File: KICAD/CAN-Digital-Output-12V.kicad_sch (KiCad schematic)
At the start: 26 parts, among them J1 UPDI Header, J2 Conn_01x04_Female, J3 UART Header, U1 AZ1117-5.0, U2 MCP2551-I-SN, U3 ATtiny414-SS, U5 MCP2515-xSO, Y1 8MHz

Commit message: Design review with Jarrod
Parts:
- added J4: 0367831201, 0367831201:MOLEX_0367831201, symbol 0367831201:0367831201
- added R10, R6, R8, R9: 1K, Resistor_SMD:R_0603_1608Metric_Pad0.98x0.95mm_HandSolder, symbol Device:R
- added U4, U6, U7, U8: VNL5050N3TR-E, Package_TO_SOT_SMD:SOT-223, symbol VNL5050N3TR-E:VNL5050N3TR-E
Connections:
- net CAN_H: now also J4.11
- net CAN_L: now also J4.12
- net GND: now also J4.4, J4.5, J4.6, U4.3 (SOURCE), U6.3 (SOURCE), U7.3 (SOURCE), U8.3 (SOURCE)
- net OUT_1: now also R6.1
- net OUT_2: now also R8.1
- net OUT_3: now also R9.1
- net OUT_4: now also R10.1
- net VCC: now also J4.1, J4.2, J4.3
- new net: R6.2, U4.1 (INPUT)
- new net: R8.2, U6.1 (INPUT)
- new net: R9.2, U7.1 (INPUT)
- new net: R10.2, U8.1 (INPUT)
- new net DO_1: J4.7, U4.2 (DRAIN), U4.4 (DRAIN)
- new net DO_2: J4.8, U6.2 (DRAIN), U6.4 (DRAIN)
- new net DO_3: J4.9, U7.2 (DRAIN), U7.4 (DRAIN)
- new net DO_4: J4.10, U8.2 (DRAIN), U8.4 (DRAIN)
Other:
- note added: "* Add LED indicator for Switches"
- note removed: "* Add LED indicator for Relays"
- moved on the sheet: H1, H2, H3, H4

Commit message: Third Design Review
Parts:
- removed J2: Conn_01x04_Female, Connector_PinHeader_1.27mm:PinHeader_1x04_P1.27mm_Vertical, symbol Connector:Conn_01x04_Female
- added D1, D2, D3, D4: LED, LED_SMD:LED_0603_1608Metric_Pad1.05x0.95mm_HandSolder, symbol Device:LED
- added R11, R12, R13, R14: 150, Resistor_SMD:R_0603_1608Metric_Pad0.98x0.95mm_HandSolder, symbol Device:R
- added S1: 219-4MSTR, 219-4MSTR:SOP254P991X385-8N, symbol 219-4MSTR:219-4MSTR
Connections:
- net GND: now also R11.1, R12.1, R13.1, R14.1
- net OUT_1: now also D1.2 (A)
- net OUT_2: now also D2.2 (A)
- net OUT_3: now also D3.2 (A)
- net OUT_4: now also D4.2 (A)
- new net: D1.1 (K), R11.2
- new net: D3.1 (K), R13.2
- new net: D2.1 (K), R12.2
- new net: D4.1 (K), R14.2
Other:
- note removed: "* Add new Connector for Power Input and CAN Input"

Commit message: V1 Schematic and Placement Design complete
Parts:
- removed H3, H4: MountingHole, MountingHole:MountingHole_2.2mm_M2_ISO14580, symbol Mechanical:MountingHole
- added R15, R16, R17, R18, R19: ?, Resistor_SMD:R_0603_1608Metric_Pad0.98x0.95mm_HandSolder, symbol Device:R
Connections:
- net +5V: now also S1.1, S1.2, S1.3, S1.4
- net CAN_H: now also J4.1; no longer J4.11
- net CAN_L: now also J4.2; no longer J4.12
- net DO_1: now also J4.6; no longer J4.7
- net DO_2: now also J4.5; no longer J4.8
- net DO_3: now also J4.4; no longer J4.9
- net DO_4: now also J4.3; no longer J4.10
- net GND: now also J4.10, J4.11, J4.12, R19.1; no longer J4.4, J4.5, J4.6
- net OUT_4: now also U3.6 (PB3); no longer U3.5 (PA7)
- net VCC: now also J4.7, J4.8, J4.9; no longer J4.1, J4.2, J4.3
- net at S1.5: now also R18.2
- net at S1.6: now also R17.2
- net at S1.7: now also R16.2
- net at S1.8: now also R15.2
- net UART_RX: no longer names the net of J3.2 (Pin_2)
- net UART_RX: no longer U3.6 (PB3)
- new net DIP: R15.1, R16.1, R17.1, R18.1, R19.2, U3.5 (PA7)
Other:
- moved on the sheet: J4, S1

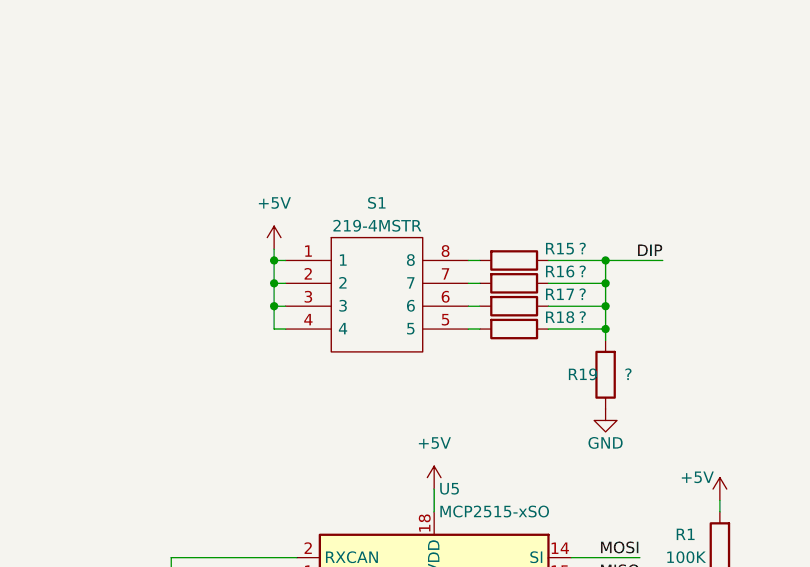
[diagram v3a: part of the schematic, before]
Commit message: Added rotary switch
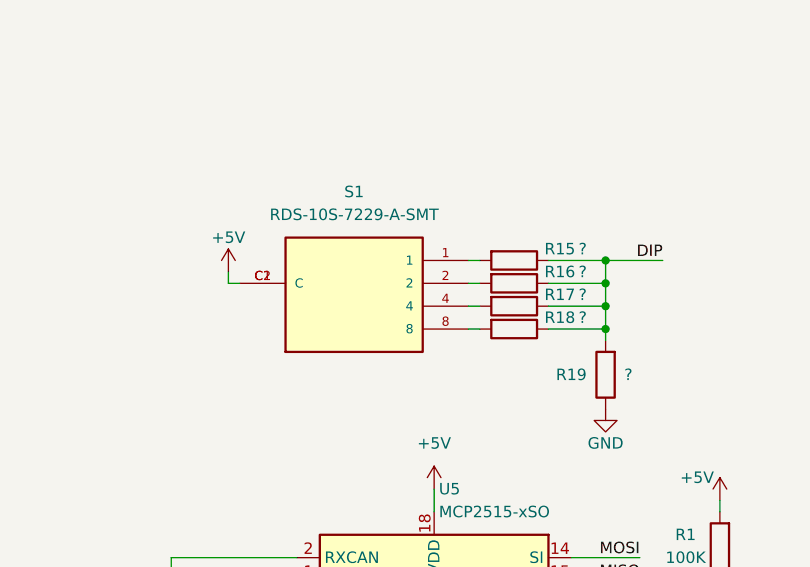
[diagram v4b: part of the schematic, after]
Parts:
- removed S1: 219-4MSTR, 219-4MSTR:SOP254P991X385-8N, symbol 219-4MSTR:219-4MSTR
- added S1: RDS-10S-7229-A-SMT, RDS-10S-7229-A-SMT:SW_RDS-10S-7229-A-SMT, symbol RDS-10S-7229-A-SMT:RDS-10S-7229-A-SMT
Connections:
- net +5V: now also S1.C1 (C), S1.C2 (C)
- net at R16.2: now also S1.2
- net at R15.2: now also S1.1
- net at R18.2: now also S1.8
- net at R17.2: now also S1.4
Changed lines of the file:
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@@
   (junction (at 173.99 72.39) (diameter 0) (color 0 0 0 0)
   )
-  (junction (at 106.68 109.22) (diameter 0) (color 0 0 0 0)
-  )
   (junction (at 217.17 29.21) (diameter 0) (color 0 0 0 0)
   )
   (junction (at 45.72 38.1) (diameter 0) (color 0 0 0 0)
   )
-  (junction (at 106.68 106.68) (diameter 0) (color 0 0 0 0)
-  )
   (junction (at 20.32 26.67) (diameter 0) (color 0 0 0 0)
   )
@@
   (junction (at 153.67 180.34) (diameter 0) (color 0 0 0 0)
   )
-  (junction (at 106.68 111.76) (diameter 0) (color 0 0 0 0)
-  )
   (no_connect (at 139.7 165.1))
   (no_connect (at 73.66 157.48))
   (no_connect (at 109.22 160.02))
   (no_connect (at 109.22 157.48))
-  (wire (pts (xy 106.68 106.68) (xy 107.95 106.68))
+  (wire (pts (xy 101.6 109.22) (xy 102.87 109.22))
     (stroke (width 0) (type default) (color 0 0 0 0))
   )
@@
     (stroke (width 0) (type default) (color 0 0 0 0))
   )
-  (wire (pts (xy 106.68 114.3) (xy 106.68 111.76))
-    (stroke (width 0) (type default) (color 0 0 0 0))
-  )
   (wire (pts (xy 78.74 167.64) (xy 82.55 167.64))
     (stroke (width 0) (type default) (color 0 0 0 0))
@@
     (stroke (width 0) (type default) (color 0 0 0 0))
   )
-  (wire (pts (xy 106.68 109.22) (xy 106.68 106.68))
-    (stroke (width 0) (type default) (color 0 0 0 0))
-  )
   (wire (pts (xy 273.05 52.07) (xy 281.94 52.07))
     (stroke (width 0) (type default) (color 0 0 0 0))
@@
     (stroke (width 0) (type default) (color 0 0 0 0))
   )
-  (wire (pts (xy 107.95 111.76) (xy 106.68 111.76))
-    (stroke (width 0) (type default) (color 0 0 0 0))
-  )
   (wire (pts (xy 224.79 31.75) (xy 224.79 39.37))
     (stroke (width 0) (type default) (color 0 0 0 0))
@@
     (stroke (width 0) (type default) (color 0 0 0 0))
   )
-  (wire (pts (xy 107.95 114.3) (xy 106.68 114.3))
-    (stroke (width 0) (type default) (color 0 0 0 0))
-  )
   (wire (pts (xy 33.02 38.1) (xy 45.72 38.1))
     (stroke (width 0) (type default) (color 0 0 0 0))
@@
     (stroke (width 0) (type default) (color 0 0 0 0))
   )
-  (wire (pts (xy 107.95 109.22) (xy 106.68 109.22))
-    (stroke (width 0) (type default) (color 0 0 0 0))
-  )
   (wire (pts (xy 160.02 180.34) (xy 153.67 180.34))
     (stroke (width 0) (type default) (color 0 0 0 0))
@@
     (stroke (width 0) (type default) (color 0 0 0 0))
   )
-  (wire (pts (xy 106.68 109.22) (xy 106.68 111.76))
-    (stroke (width 0) (type default) (color 0 0 0 0))
-  )
   (wire (pts (xy 20.32 35.56) (xy 20.32 38.1))
     (stroke (width 0) (type default) (color 0 0 0 0))
@@
     (stroke (width 0) (type default) (color 0 0 0 0))
   )
-  (wire (pts (xy 106.68 105.41) (xy 106.68 106.68))
+  (wire (pts (xy 101.6 107.95) (xy 101.6 109.22))
     (stroke (width 0) (type default) (color 0 0 0 0))
   )
@@
   (symbol (lib_id "Device:R") (at 143.51 119.38 180) (unit 1)
     (in_bom yes) (on_board yes)
-    (property "Reference" "R19" (id 0) (at 140.97 119.38 0))
+    (property "Reference" "R19" (id 0) (at 139.7 119.38 0))
     (property "Value" "?" (id 1) (at 146.05 119.38 0))
     (property "Footprint" "Resistor_SMD:R_0603_1608Metric_Pad0.98x0.95mm_HandSolder" (id 2) (at 145.288 119.38 90)
@@
     (pin "8")
   )
+  (symbol (lib_id "RDS-10S-7229-A-SMT:RDS-10S-7229-A-SMT") (at 115.57 111.76 0) (unit 1)
+    (in_bom yes) (on_board yes) (fields_autoplaced)
+    (property "Reference" "S1" (id 0) (at 115.57 99.06 0))
+    (property "Value" "RDS-10S-7229-A-SMT" (id 1) (at 115.57 101.6 0))
+    (property "Footprint" "RDS-10S-7229-A-SMT:SW_RDS-10S-7229-A-SMT" (id 2) (at 115.57 111.76 0)
+      (effects (font (size 1.27 1.27)) (justify bottom) hide)
+    )
+    (property "Datasheet" "" (id 3) (at 115.57 111.76 0)
+      (effects (font (size 1.27 1.27)) hide)
+    )
+    (property "MANUFACTURER" "CUI Devices" (id 4) (at 115.57 111.76 0)
+      (effects (font (size 1.27 1.27)) (justify bottom) hide)
+    )
+    (property "PARTREV" "1.0" (id 5) (at 115.57 111.76 0)
+      (effects (font (size 1.27 1.27)) (justify bottom) hide)
+    )
+    (property "MAXIMUM_PACKAGE_HEIGHT" "3 mm" (id 6) (at 115.57 111.76 0)
+      (effects (font (size 1.27 1.27)) (justify bottom) hide)
+    )
+    (property "STANDARD" "Manufacturer Recommendations" (id 7) (at 115.57 111.76 0)
+      (effects (font (size 1.27 1.27)) (justify bottom) hide)
+    )
+    (pin "1")
+    (pin "2")
+    (pin "4")
+    (pin "8")
+    (pin "C1")
+    (pin "C2")
+  )
   (symbol (lib_id "Mechanical:MountingHole") (at 26.67 90.17 0) (unit 1)
     (in_bom yes) (on_board yes) (fields_autoplaced)
@@
     (pin "1")
   )
-  (symbol (lib_id "power:+5V") (at 106.68 105.41 0) (unit 1)
-    (in_bom yes) (on_board yes) (fields_autoplaced)
-    (property "Reference" "#PWR0114" (id 0) (at 106.68 109.22 0)
+  (symbol (lib_id "power:+5V") (at 101.6 107.95 0) (unit 1)
+    (in_bom yes) (on_board yes)
+    (property "Reference" "#PWR0114" (id 0) (at 101.6 111.76 0)
       (effects (font (size 1.27 1.27)) hide)
     )
-    (property "Value" "+5V" (id 1) (at 106.68 100.33 0))
-    (property "Footprint" "" (id 2) (at 106.68 105.41 0)
+    (property "Value" "+5V" (id 1) (at 101.6 104.14 0))
+    (property "Footprint" "" (id 2) (at 101.6 107.95 0)
       (effects (font (size 1.27 1.27)) hide)
     )
-    (property "Datasheet" "" (id 3) (at 106.68 105.41 0)
+    (property "Datasheet" "" (id 3) (at 101.6 107.95 0)
       (effects (font (size 1.27 1.27)) hide)
     )
@@
     (pin "1")
   )
-  (symbol (lib_id "219-4MSTR:219-4MSTR") (at 107.95 106.68 0) (unit 1)
-    (in_bom yes) (on_board yes)
-    (property "Reference" "S1" (id 0) (at 118.11 100.33 0))
-    (property "Value" "219-4MSTR" (id 1) (at 118.11 102.87 0))
-    (property "Footprint" "219-4MSTR:SOP254P991X385-8N" (id 2) (at 124.46 104.14 0)
-      (effects (font (size 1.27 1.27)) (justify left) hide)
-    )
-    (property "Datasheet" "https://www.ctscorp.com/wp-content/uploads/219.pdf" (id 3) (at 124.46 106.68 0)
-      (effects (font (size 1.27 1.27)) (justify left) hide)
-    )
-    (property "Description" "DIP Switches / SIP Switches SPST 4 switch sections" (id 4) (at 124.46 109.22 0)
-      (effects (font (size 1.27 1.27)) (justify left) hide)
-    )
-    (property "Height" "3.85" (id 5) (at 124.46 111.76 0)
-      (effects (font (size 1.27 1.27)) (justify left) hide)
-    )
-    (property "Manufacturer_Name" "CTS" (id 6) (at 124.46 114.3 0)
-      (effects (font (size 1.27 1.27)) (justify left) hide)
-    )
-    (property "Manufacturer_Part_Number" "219-4MSTR" (id 7) (at 124.46 116.84 0)
-      (effects (font (size 1.27 1.27)) (justify left) hide)
-    )
-    (property "Mouser Part Number" "774-2194MSTR" (id 8) (at 124.46 119.38 0)
-      (effects (font (size 1.27 1.27)) (justify left) hide)
-    )
-    (property "Mouser Price/Stock" "https://www.mouser.co.uk/ProductDetail/CTS-Electronic-Components/219-4MSTR?qs=qNzHFtQhdJ9B7GDGaS2NPg%3D%3D" (id 9) (at 124.46 121.92 0)
-      (effects (font (size 1.27 1.27)) (justify left) hide)
-    )
-    (property "Arrow Part Number" "219-4MSTR" (id 10) (at 124.46 124.46 0)
-      (effects (font (size 1.27 1.27)) (justify left) hide)
-    )
-    (property "Arrow Price/Stock" "https://www.arrow.com/en/products/219-4mstr/cts" (id 11) (at 124.46 127 0)
-      (effects (font (size 1.27 1.27)) (justify left) hide)
-    )
-    (property "Digi-Key Link" "https://www.digikey.com/en/products/detail/cts-electrocomponents/219-4MSTR/480303" (id 12) (at 107.95 106.68 0)
-      (effects (font (size 1.27 1.27)) hide)
-    )
-    (property "Digi-Key PN" "CT3117CT-ND" (id 13) (at 107.95 106.68 0)
-      (effects (font (size 1.27 1.27)) hide)
-    )
-    (property "Manufacturer PN" "219-4MSTR" (id 14) (at 107.95 106.68 0)
-      (effects (font (size 1.27 1.27)) hide)
-    )
-    (property "Price" "0.91" (id 15) (at 107.95 106.68 0)
-      (effects (font (size 1.27 1.27)) hide)
-    )
-    (pin "1")
-    (pin "2")
-    (pin "3")
-    (pin "4")
-    (pin "5")
-    (pin "6")
-    (pin "7")
-    (pin "8")
-  )
   (symbol (lib_id "VNL5050N3TR-E:VNL5050N3TR-E") (at 228.6 100.33 0) (unit 1)
     (in_bom yes) (on_board yes)
@@
       (reference "R19") (unit 1) (value "?") (footprint "Resistor_SMD:R_0603_1608Metric_Pad0.98x0.95mm_HandSolder")
     )
-    (path "/ac9888d6-baac-4b8e-8475-c67b0e693c19"
-      (reference "S1") (unit 1) (value "219-4MSTR") (footprint "219-4MSTR:SOP254P991X385-8N")
+    (path "/29df67e7-4b69-4430-b947-5e23b1ae6fc1"
+      (reference "S1") (unit 1) (value "RDS-10S-7229-A-SMT") (footprint "RDS-10S-7229-A-SMT:SW_RDS-10S-7229-A-SMT")
     )
     (path "/6ed73bae-4682-4ede-9d82-100d151ac456"

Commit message: Sent to Fab
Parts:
- removed J1: UPDI Header, Connector_PinHeader_1.27mm:PinHeader_1x02_P1.27mm_Vertical, symbol Connector:Conn_01x02_Female
- J3: value UART Header -> UPDI Header
- J4: Digi-Key Link (none) -> https://www.digikey.com/en/products/detail/molex/0367831201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; Digi-Key PN (none) -> WM9330-ND; Manufacturer PN (none) -> 0367831201; Price (none) -> 1.65
- R10, R6, R8, R9: Digi-Key Link (none) -> https://www.digikey.com/en/products/detail/yageo/RC0603FR-0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; Digi-Key PN (none) -> 311-1.00KHRCT-ND; Manufacturer PN (none) -> RC0603FR-071KL; Price (none) -> 0.10
- S1: Digi-Key Link (none) -> https://www.digikey.com/en/products/detail/cui-devices/RDS-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; Digi-Key PN (none) -> 2223-RDS-10S-7229-A-SMT-ND; Manufacturer PN (none) -> RDS-10S-7229-A-SMT; Price (none) -> 2.92
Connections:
- net UART_TX: now also J3.2 (Pin_2); no longer J3.3 (Pin_3)
- net at R7.1: now also J3.3 (Pin_3)
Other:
- note removed: "* Add LED indicator for Switches"
- note removed: "* DIP Swtiches to Change Modes (CAN Speed, CAN ID, Others...)"
- note removed: "* Design so that system can be programmed easier with Arduino Nanao"
- note removed: "* Determine if simple SPST output, or 12V and GND output"

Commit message: V1 Software is fully functional
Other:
- note added: "* 10uF Missing from Order"
- note added: "* 4.7K is wrongly an 0402 part, should be 0604"
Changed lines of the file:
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@@
     (effects (font (size 3.5 3.5)) (justify left bottom))
+  )
+  (text "* 4.7K is wrongly an 0402 part, should be 0604" (at 143.51 100.33 0)
+    (effects (font (size 1.5 1.5)) (justify left bottom))
+  )
+  (text "* 10uF Missing from Order\n" (at 143.51 97.79 0)
+    (effects (font (size 1.5 1.5)) (justify left bottom))
   )
   (text "* Add Test points" (at 199.39 140.97 0)
